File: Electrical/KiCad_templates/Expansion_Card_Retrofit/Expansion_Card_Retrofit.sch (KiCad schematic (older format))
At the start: 5 parts, among them P1 USB_C_Plug_USB2.0, U1 AP2112K-3.3

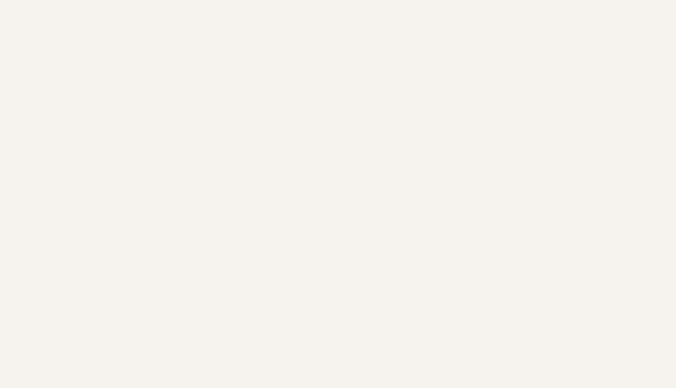
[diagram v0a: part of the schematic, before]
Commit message: Update test points
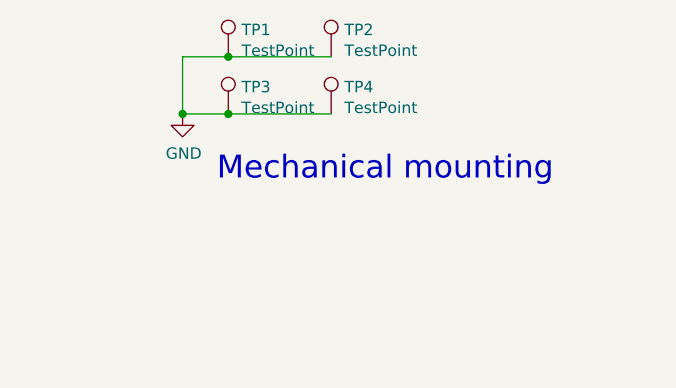
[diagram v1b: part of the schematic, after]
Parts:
- added TP1, TP2, TP3, TP4: TestPoint, TestPoint:TestPoint_Pad_1.5x1.5mm, symbol Connector:TestPoint
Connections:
- net GND: now also TP1.1, TP2.1, TP3.1, TP4.1
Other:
- note added: "Mechanical mounting"
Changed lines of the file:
@@
 Wire Wire Line
 	2250 1500 2900 1500
+Wire Wire Line
+	9200 900  9200 1150
+Connection ~ 9200 1150
+$Comp
+L power:GND #PWR0101
+U 1 1 606A9B9C
+P 9200 1150
+F 0 "#PWR0101" H 9200 900 50  0001 C CNN
+F 1 "GND" H 9205 977 50  0000 C CNN
+F 2 "" H 9200 1150 50  0001 C CNN
+F 3 "" H 9200 1150 50  0001 C CNN
+	1    9200 1150
+	1    0    0    -1
+$EndComp
+Text Notes 9350 1450 0    100  ~ 0
+Mechanical mounting
+Wire Wire Line
+	9400 1150 9200 1150
+Wire Wire Line
+	9850 1150 9400 1150
+Connection ~ 9400 1150
+Wire Wire Line
+	9400 900  9200 900
+Wire Wire Line
+	9850 900  9400 900
+Connection ~ 9400 900
+$Comp
+L Connector:TestPoint TP4
+U 1 1 606A8E98
+P 9850 1150
+F 0 "TP4" H 9908 1268 50  0000 L CNN
+F 1 "TestPoint" H 9908 1177 50  0000 L CNN
+F 2 "TestPoint:TestPoint_Pad_1.5x1.5mm" H 10050 1150 50  0001 C CNN
+F 3 "~" H 10050 1150 50  0001 C CNN
+	1    9850 1150
+	1    0    0    -1
+$EndComp
+$Comp
+L Connector:TestPoint TP3
+U 1 1 606A8C9B
+P 9400 1150
+F 0 "TP3" H 9458 1268 50  0000 L CNN
+F 1 "TestPoint" H 9458 1177 50  0000 L CNN
+F 2 "TestPoint:TestPoint_Pad_1.5x1.5mm" H 9600 1150 50  0001 C CNN
+F 3 "~" H 9600 1150 50  0001 C CNN
+	1    9400 1150
+	1    0    0    -1
+$EndComp
+$Comp
+L Connector:TestPoint TP2
+U 1 1 606A78C1
+P 9850 900
+F 0 "TP2" H 9908 1018 50  0000 L CNN
+F 1 "TestPoint" H 9908 927 50  0000 L CNN
+F 2 "TestPoint:TestPoint_Pad_1.5x1.5mm" H 10050 900 50  0001 C CNN
+F 3 "~" H 10050 900 50  0001 C CNN
+	1    9850 900
+	1    0    0    -1
+$EndComp
+$Comp
+L Connector:TestPoint TP1
+U 1 1 606A89A3
+P 9400 900
+F 0 "TP1" H 9458 1018 50  0000 L CNN
+F 1 "TestPoint" H 9458 927 50  0000 L CNN
+F 2 "TestPoint:TestPoint_Pad_1.5x1.5mm" H 9600 900 50  0001 C CNN
+F 3 "~" H 9600 900 50  0001 C CNN
+	1    9400 900
+	1    0    0    -1
+$EndComp
 $EndSCHEMATC
